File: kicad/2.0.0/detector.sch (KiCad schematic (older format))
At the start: 65 parts, among them U1 LM317, U2 LM337, U3 REF5010ID, U4 OPA2197xD, U5 OPA2197xD

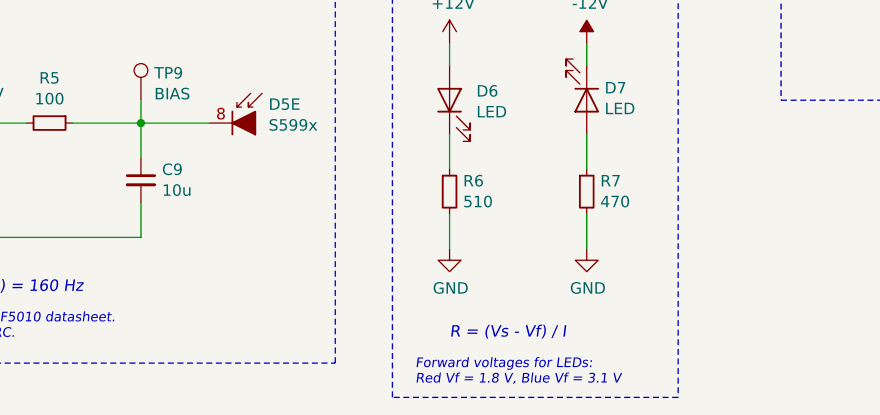
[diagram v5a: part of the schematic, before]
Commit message: grouped components of detector 2.0.0 pcb
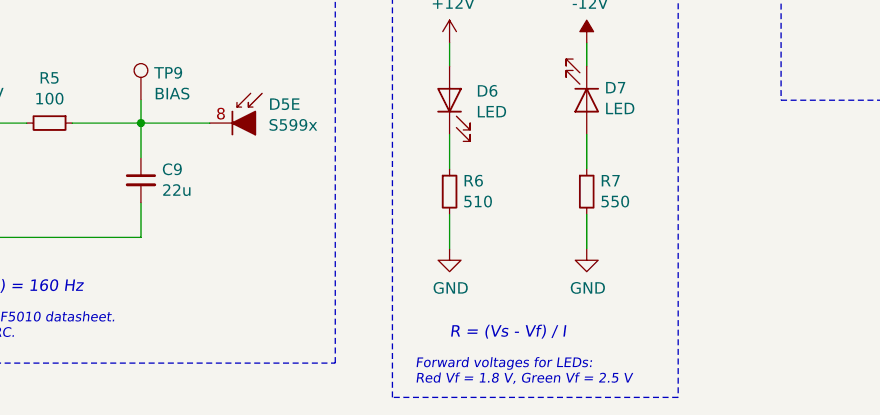
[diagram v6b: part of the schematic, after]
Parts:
- C9: value 10u -> 22u
- D6, D7: footprint Diode_SMD:D_0805_2012Metric -> Diode_SMD:D_0603_1608Metric
- R7: value 470 -> 550
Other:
- note added: "Forward voltages for LEDs:\nRed Vf = 1.8 V, Green Vf = 2.5 V"
- note removed: "Forward voltages for LEDs:\nRed Vf = 1.8 V, Blue Vf = 3.1 V"
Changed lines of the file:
@@
 Text Notes 750  5400 0    50   ~ 0
 REVERSE BIAS REFERENCE
-Text Notes 5050 5400 0    50   ~ 0
-POWER LEDS
-Wire Notes Line
-	5050 5450 6300 5450
-$Comp
-L power:-12V #PWR010
-U 1 1 5E96D511
-P 5900 5750
-F 0 "#PWR010" H 5900 5850 50  0001 C CNN
-F 1 "-12V" H 5915 5923 50  0000 C CNN
-F 2 "" H 5900 5750 50  0001 C CNN
-F 3 "" H 5900 5750 50  0001 C CNN
-	1    5900 5750
-	1    0    0    -1
-$EndComp
-Wire Wire Line
-	5900 6500 5900 6650
-Wire Wire Line
-	5900 6150 5900 6300
-$Comp
-L Device:R_Small R?
-U 1 1 5E96D519
-P 5900 6400
-AR Path="/5E48BEC6/5E96D519" Ref="R?"  Part="1"
-AR Path="/5E4BE137/5E96D519" Ref="R?"  Part="1"
-AR Path="/5E96D519" Ref="R7"  Part="1"
-F 0 "R7" H 5959 6446 50  0000 L CNN
-F 1 "470" H 5959 6355 50  0000 L CNN
-F 2 "Resistor_SMD:R_0603_1608Metric" H 5900 6400 50  0001 C CNN
-F 3 "~" H 5900 6400 50  0001 C CNN
-	1    5900 6400
-	1    0    0    -1
-$EndComp
-Wire Wire Line
-	5900 5750 5900 5850
-$Comp
-L power:GND #PWR011
-U 1 1 5E96D520
-P 5900 6650
-F 0 "#PWR011" H 5900 6400 50  0001 C CNN
-F 1 "GND" H 5905 6477 50  0000 C CNN
-F 2 "" H 5900 6650 50  0001 C CNN
-F 3 "" H 5900 6650 50  0001 C CNN
-	1    5900 6650
-	1    0    0    -1
-$EndComp
-$Comp
-L Device:LED D7
-U 1 1 5E96D526
-P 5900 6000
-F 0 "D7" V 5847 6078 50  0000 L CNN
-F 1 "LED" V 5938 6078 50  0000 L CNN
-F 2 "Diode_SMD:D_0805_2012Metric" H 5900 6000 50  0001 C CNN
-F 3 "~" H 5900 6000 50  0001 C CNN
-	1    5900 6000
-	0    1    1    0
-$EndComp
-Wire Wire Line
-	5300 6500 5300 6650
-Wire Wire Line
-	5300 6150 5300 6300
-$Comp
-L Device:R_Small R?
-U 1 1 5E96D52E
-P 5300 6400
-AR Path="/5E48BEC6/5E96D52E" Ref="R?"  Part="1"
-AR Path="/5E4BE137/5E96D52E" Ref="R?"  Part="1"
-AR Path="/5E96D52E" Ref="R6"  Part="1"
-F 0 "R6" H 5359 6446 50  0000 L CNN
-F 1 "510" H 5359 6355 50  0000 L CNN
-F 2 "Resistor_SMD:R_0603_1608Metric" H 5300 6400 50  0001 C CNN
-F 3 "~" H 5300 6400 50  0001 C CNN
-	1    5300 6400
-	1    0    0    -1
-$EndComp
-Wire Wire Line
-	5300 5750 5300 5850
-$Comp
-L power:GND #PWR09
-U 1 1 5E96D535
-P 5300 6650
-F 0 "#PWR09" H 5300 6400 50  0001 C CNN
-F 1 "GND" H 5305 6477 50  0000 C CNN
-F 2 "" H 5300 6650 50  0001 C CNN
-F 3 "" H 5300 6650 50  0001 C CNN
-	1    5300 6650
-	1    0    0    -1
-$EndComp
-$Comp
-L Device:LED D6
-U 1 1 5E96D53B
-P 5300 6000
-F 0 "D6" V 5339 5883 50  0000 R CNN
-F 1 "LED" V 5248 5883 50  0000 R CNN
-F 2 "Diode_SMD:D_0805_2012Metric" H 5300 6000 50  0001 C CNN
-F 3 "~" H 5300 6000 50  0001 C CNN
-	1    5300 6000
-	0    -1   -1   0
-$EndComp
-$Comp
-L power:+12V #PWR?
-U 1 1 5E96D541
-P 5300 5750
-AR Path="/5E48BEC6/5E96D541" Ref="#PWR?"  Part="1"
-AR Path="/5E4BE137/5E96D541" Ref="#PWR?"  Part="1"
-AR Path="/5E96D541" Ref="#PWR08"  Part="1"
-F 0 "#PWR08" H 5300 5600 50  0001 C CNN
-F 1 "+12V" H 5315 5923 50  0000 C CNN
-F 2 "" H 5300 5750 50  0001 C CNN
-F 3 "" H 5300 5750 50  0001 C CNN
-	1    5300 5750
-	1    0    0    -1
-$EndComp
 $Comp
 L Sensor_Optical_Position:S599x D5
@@
 P 3950 6350
 F 0 "C9" H 4042 6396 50  0000 L CNN
-F 1 "10u" H 4042 6305 50  0000 L CNN
+F 1 "22u" H 4042 6305 50  0000 L CNN
 F 2 "Capacitor_SMD:C_1206_3216Metric" H 3950 6350 50  0001 C CNN
 F 3 "~" H 3950 6350 50  0001 C CNN
@@
 	1    0    0    -1
 $EndComp
-Wire Notes Line
-	6300 5450 6300 7300
-Wire Notes Line
-	6300 7300 5050 7300
-Wire Notes Line
-	5050 7300 5050 5450
-Text Notes 5300 7050 0    50   Italic 0
-R = (Vs - Vf) / I
-Text Notes 5150 7250 0    42   Italic 0
-Forward voltages for LEDs:\nRed Vf = 1.8 V, Blue Vf = 3.1 V
 Wire Wire Line
 	1250 6550 1250 6600
@@
 	1    0    0    -1
 $EndComp
+Text Notes 5150 7250 0    42   Italic 0
+Forward voltages for LEDs:\nRed Vf = 1.8 V, Green Vf = 2.5 V
+Text Notes 5300 7050 0    50   Italic 0
+R = (Vs - Vf) / I
+Wire Notes Line
+	5050 7300 5050 5450
+Wire Notes Line
+	6300 7300 5050 7300
+Wire Notes Line
+	6300 5450 6300 7300
+$Comp
+L power:+12V #PWR?
+U 1 1 5E96D541
+P 5300 5750
+AR Path="/5E48BEC6/5E96D541" Ref="#PWR?"  Part="1"
+AR Path="/5E4BE137/5E96D541" Ref="#PWR?"  Part="1"
+AR Path="/5E96D541" Ref="#PWR08"  Part="1"
+F 0 "#PWR08" H 5300 5600 50  0001 C CNN
+F 1 "+12V" H 5315 5923 50  0000 C CNN
+F 2 "" H 5300 5750 50  0001 C CNN
+F 3 "" H 5300 5750 50  0001 C CNN
+	1    5300 5750
+	1    0    0    -1
+$EndComp
+$Comp
+L Device:LED D6
+U 1 1 5E96D53B
+P 5300 6000
+F 0 "D6" V 5339 5883 50  0000 R CNN
+F 1 "LED" V 5248 5883 50  0000 R CNN
+F 2 "Diode_SMD:D_0603_1608Metric" H 5300 6000 50  0001 C CNN
+F 3 "~" H 5300 6000 50  0001 C CNN
+	1    5300 6000
+	0    -1   -1   0
+$EndComp
+$Comp
+L power:GND #PWR09
+U 1 1 5E96D535
+P 5300 6650
+F 0 "#PWR09" H 5300 6400 50  0001 C CNN
+F 1 "GND" H 5305 6477 50  0000 C CNN
+F 2 "" H 5300 6650 50  0001 C CNN
+F 3 "" H 5300 6650 50  0001 C CNN
+	1    5300 6650
+	1    0    0    -1
+$EndComp
+Wire Wire Line
+	5300 5750 5300 5850
+$Comp
+L Device:R_Small R?
+U 1 1 5E96D52E
+P 5300 6400
+AR Path="/5E48BEC6/5E96D52E" Ref="R?"  Part="1"
+AR Path="/5E4BE137/5E96D52E" Ref="R?"  Part="1"
+AR Path="/5E96D52E" Ref="R6"  Part="1"
+F 0 "R6" H 5359 6446 50  0000 L CNN
+F 1 "510" H 5359 6355 50  0000 L CNN
+F 2 "Resistor_SMD:R_0603_1608Metric" H 5300 6400 50  0001 C CNN
+F 3 "~" H 5300 6400 50  0001 C CNN
+	1    5300 6400
+	1    0    0    -1
+$EndComp
+Wire Wire Line
+	5300 6150 5300 6300
+Wire Wire Line
+	5300 6500 5300 6650
+$Comp
+L Device:LED D7
+U 1 1 5E96D526
+P 5900 6000
+F 0 "D7" V 5847 6078 50  0000 L CNN
+F 1 "LED" V 5938 6078 50  0000 L CNN
+F 2 "Diode_SMD:D_0603_1608Metric" H 5900 6000 50  0001 C CNN
+F 3 "~" H 5900 6000 50  0001 C CNN
+	1    5900 6000
+	0    1    1    0
+$EndComp
+$Comp
+L power:GND #PWR011
+U 1 1 5E96D520
+P 5900 6650
+F 0 "#PWR011" H 5900 6400 50  0001 C CNN
+F 1 "GND" H 5905 6477 50  0000 C CNN
+F 2 "" H 5900 6650 50  0001 C CNN
+F 3 "" H 5900 6650 50  0001 C CNN
+	1    5900 6650
+	1    0    0    -1
+$EndComp
+Wire Wire Line
+	5900 5750 5900 5850
+$Comp
+L Device:R_Small R?
+U 1 1 5E96D519
+P 5900 6400
+AR Path="/5E48BEC6/5E96D519" Ref="R?"  Part="1"
+AR Path="/5E4BE137/5E96D519" Ref="R?"  Part="1"
+AR Path="/5E96D519" Ref="R7"  Part="1"
+F 0 "R7" H 5959 6446 50  0000 L CNN
+F 1 "550" H 5959 6355 50  0000 L CNN
+F 2 "Resistor_SMD:R_0603_1608Metric" H 5900 6400 50  0001 C CNN
+F 3 "~" H 5900 6400 50  0001 C CNN
+	1    5900 6400
+	1    0    0    -1
+$EndComp
+Wire Wire Line
+	5900 6150 5900 6300
+Wire Wire Line
+	5900 6500 5900 6650
+$Comp
+L power:-12V #PWR010
+U 1 1 5E96D511
+P 5900 5750
+F 0 "#PWR010" H 5900 5850 50  0001 C CNN
+F 1 "-12V" H 5915 5923 50  0000 C CNN
+F 2 "" H 5900 5750 50  0001 C CNN
+F 3 "" H 5900 5750 50  0001 C CNN
+	1    5900 5750
+	1    0    0    -1
+$EndComp
+Wire Notes Line
+	5050 5450 6300 5450
+Text Notes 5050 5400 0    50   ~ 0
+POWER LEDS
 $EndSCHEMATC

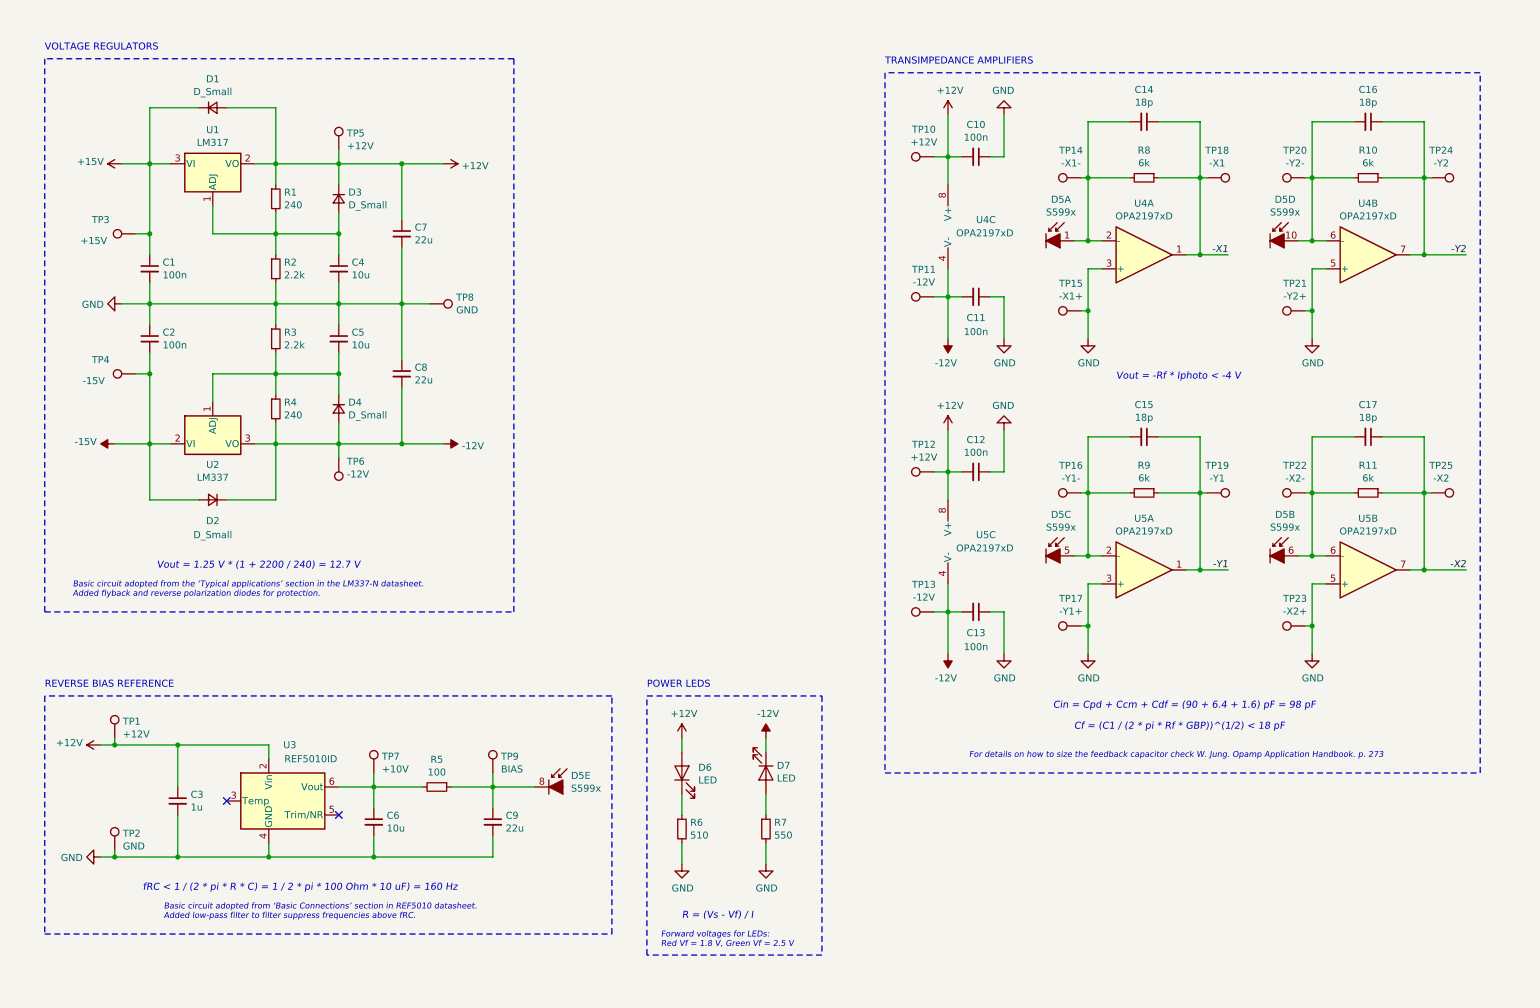
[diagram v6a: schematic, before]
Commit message: completed tracks of voltage references and regulators of 2.0.0 detector
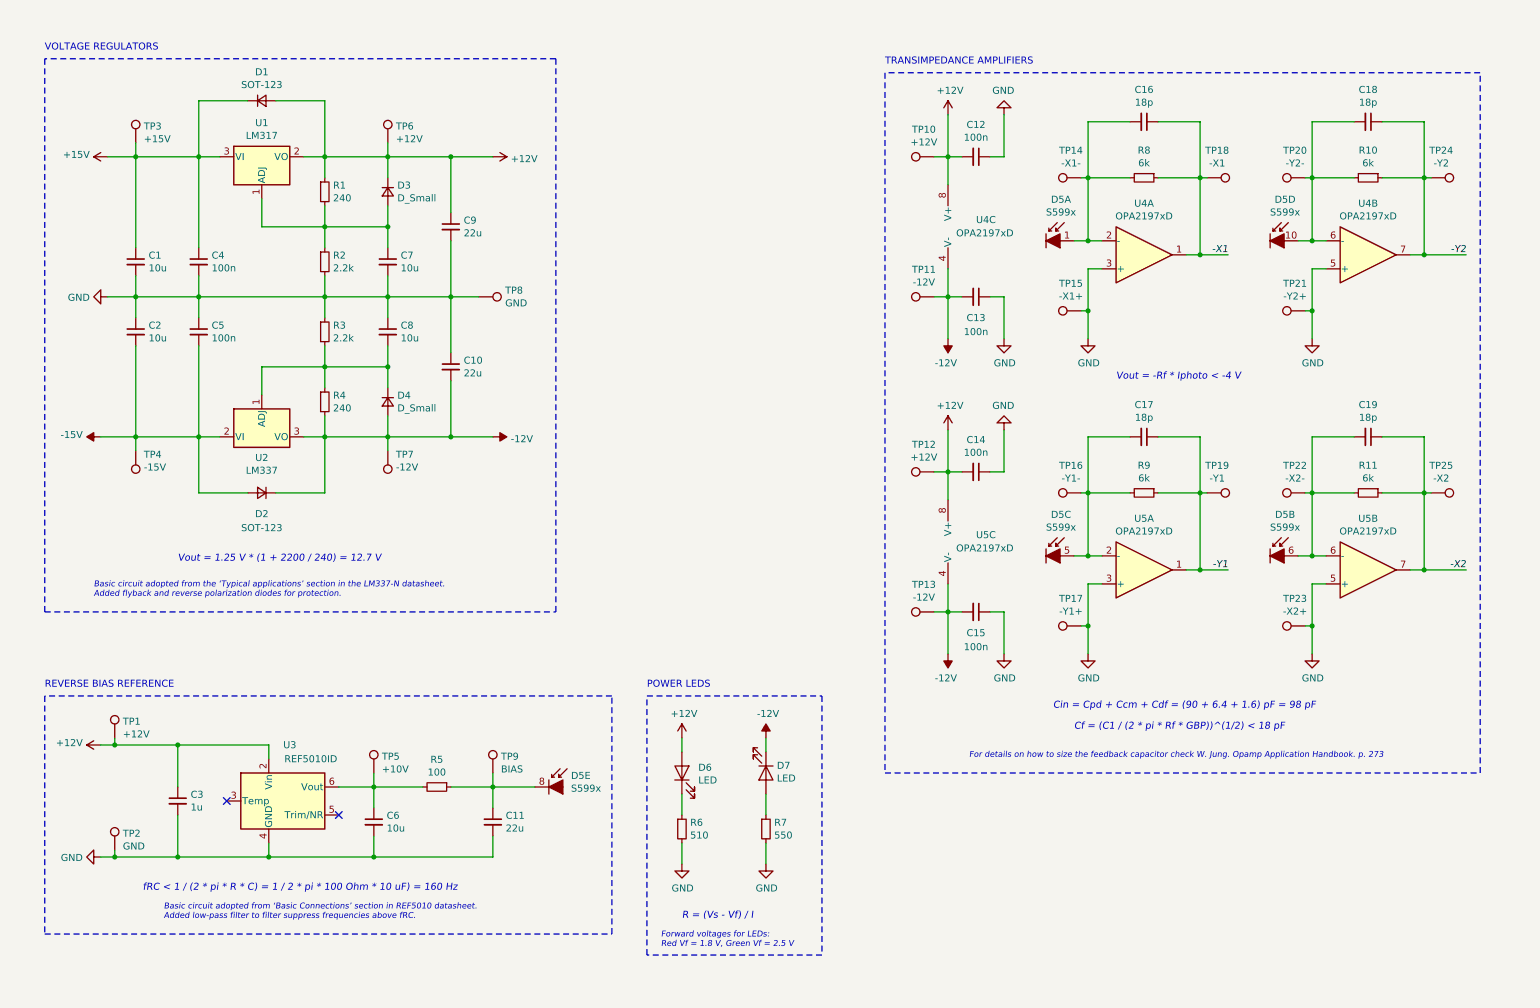
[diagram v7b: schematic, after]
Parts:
- added C1, C2: 10u, Capacitor_SMD:C_1206_3216Metric, symbol Device:C_Small
- D1, D2: value D_Small -> SOT-123
- renumbered C8 to C10, C9 to C11, C10 to C12, C11 to C13, C12 to C14, C13 to C15, C14 to C16, C15 to C17, C16 to C18, C17 to C19, C1 to C4, C2 to C5, C4 to C7, C5 to C8, C7 to C9, TP7 to TP5, TP5 to TP6, TP6 to TP7
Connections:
- net +15V: now also C1.1
- net -15V: now also C2.2
- net GND: now also C1.2, C2.1
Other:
- moved on the sheet: C10, C4, C5, C7, C8, C9, D1, D2, D3, D4, R1, R2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

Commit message: replaced voltage regulators of 2.0.0 detector with LDO regulators
Low-dropout (LDO) voltage regulators come in small packages, i.e.
SOT-23, however they are more susceptible for ringing.
The packages in which you can buy the non-LDO voltage regulators, e.g. SOIC-8 or SOT-223,
are large compared to the remaining circuitry.
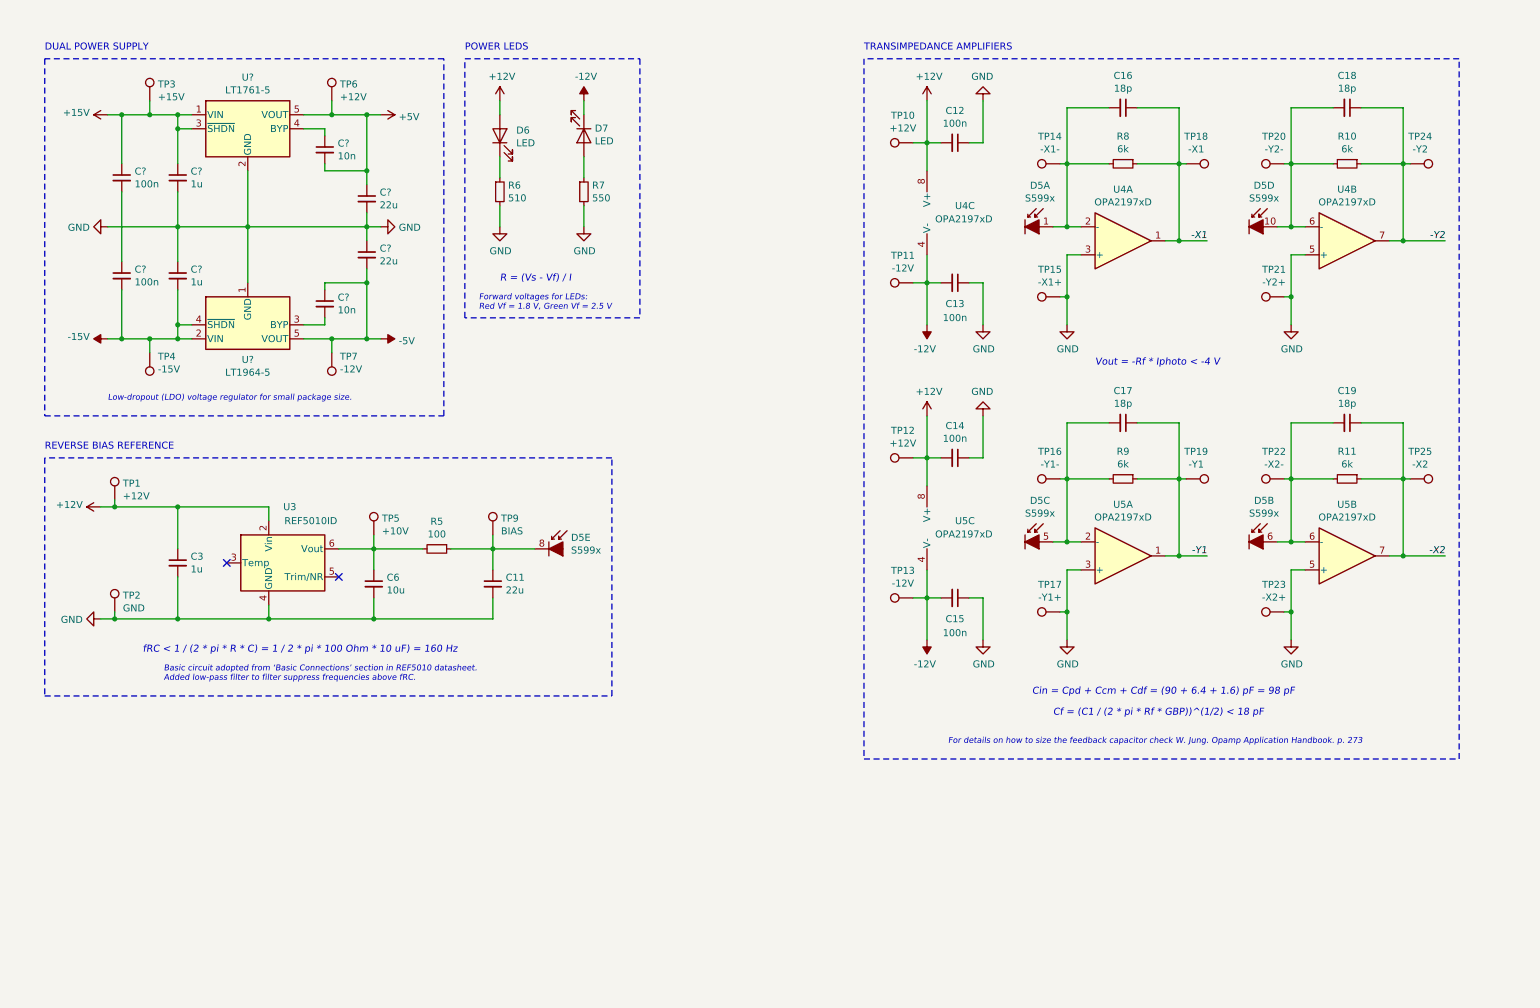
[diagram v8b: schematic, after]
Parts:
- removed C1, C2, C7, C8: 10u, Capacitor_SMD:C_1206_3216Metric, symbol Device:C_Small
- removed C10, C9: 22u, Capacitor_SMD:C_1206_3216Metric, symbol Device:C_Small
- removed C4, C5: 100n, Capacitor_SMD:C_0603_1608Metric, symbol Device:C_Small
- removed D1, D2: SOT-123, Diode_SMD:D_SOD-123, symbol Device:D_Small
- removed D3, D4: D_Small, Diode_SMD:D_SOD-123, symbol Device:D_Small
- removed R1, R4: 240, Resistor_SMD:R_0603_1608Metric, symbol Device:R_Small
- removed R2, R3: 2.2k, Resistor_SMD:R_0603_1608Metric, symbol Device:R_Small
- removed TP8: GND, TestPoint:TestPoint_Pad_D1.0mm, symbol Connector:TestPoint
- removed U1: LM317, Package_TO_SOT_SMD:SOT-223-3_TabPin2, symbol Regulator_Linear:LM317_3PinPackage
- removed U2: LM337, Package_TO_SOT_SMD:SOT-223-3_TabPin2, symbol Regulator_Linear:LM337_SOT223
- added C? (x2): 1u, Capacitor_SMD:C_1206_3216Metric, symbol Device:C_Small
- added C? (x2): 22u, Capacitor_SMD:C_1206_3216Metric, symbol Device:C_Small
- added C? (x2): 10n, Capacitor_SMD:C_1206_3216Metric, symbol Device:C_Small
- added C? (x2): 100n, Capacitor_SMD:C_1206_3216Metric, symbol Device:C_Small
- added U?: LT1964-5, Package_TO_SOT_SMD:TSOT-23-5, symbol Regulator_Linear:LT1964-5
- added U?: LT1761-5, Package_TO_SOT_SMD:TSOT-23-5, symbol Regulator_Linear:LT1761-5
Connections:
- net +12V: no longer TP6.1
- net +15V: now also C?.1, C?.1, U?.1 (VIN), U?.3 (~SHDN)
- net -12V: no longer TP7.1
- net -15V: now also C?.2, C?.2, U?.2 (VIN), U?.4 (~SHDN)
- net GND: now also C?.1, C?.1, C?.2, C?.2, U?.1 (GND), U?.2 (GND)
- new net: C?.2, U?.3 (BYP)
- new net: C?.1, U?.4 (BYP)
- new net: C?.1, C?.2
- new net +5V: C?.1, C?.2, TP6.1, U?.5 (VOUT)
- new net -5V: C?.1, C?.2, TP7.1, U?.5 (VOUT)
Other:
- note added: "DUAL POWER SUPPLY"
- note added: "Low-dropout (LDO) voltage regulator for small package size."
- note removed: "Basic circuit adopted from the ‘Typical applications’ section in the LM337-N datasheet.\nAdded flyback and reverse polarization diodes for protection."
- note removed: "VOLTAGE REGULATORS"
- note removed: "Vout = 1.25 V * (1 + 2200 / 240) = 12.7 V"
- moved on the sheet: C11, C12, C13, C14, C15, C16, C17, C18, C19, C3, C6, D5A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
